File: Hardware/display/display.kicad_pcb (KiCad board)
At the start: 2 copper layers, 30.5 x 25.4 mm, 5 parts, among them J1 CONN_01X08, J2 CONN_01X08

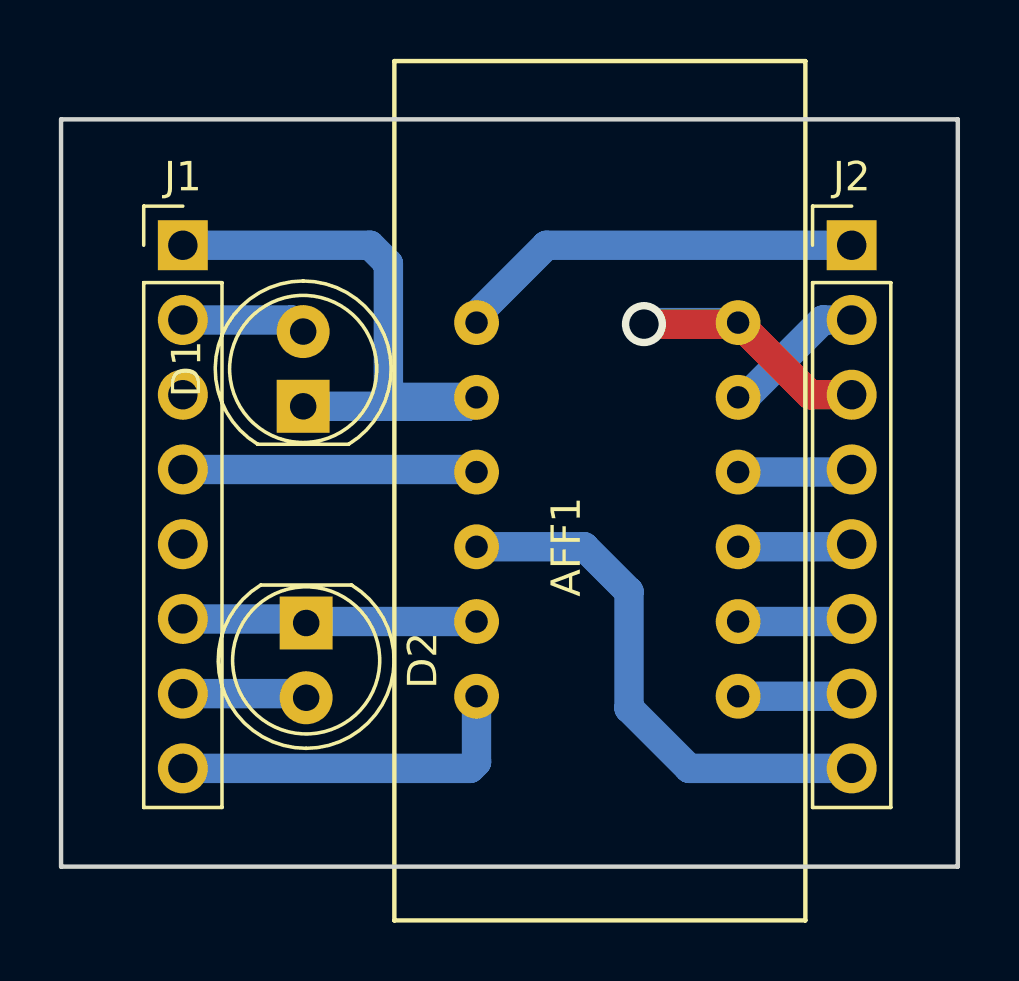
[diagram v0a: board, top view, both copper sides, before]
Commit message: Added 2 more LEDs
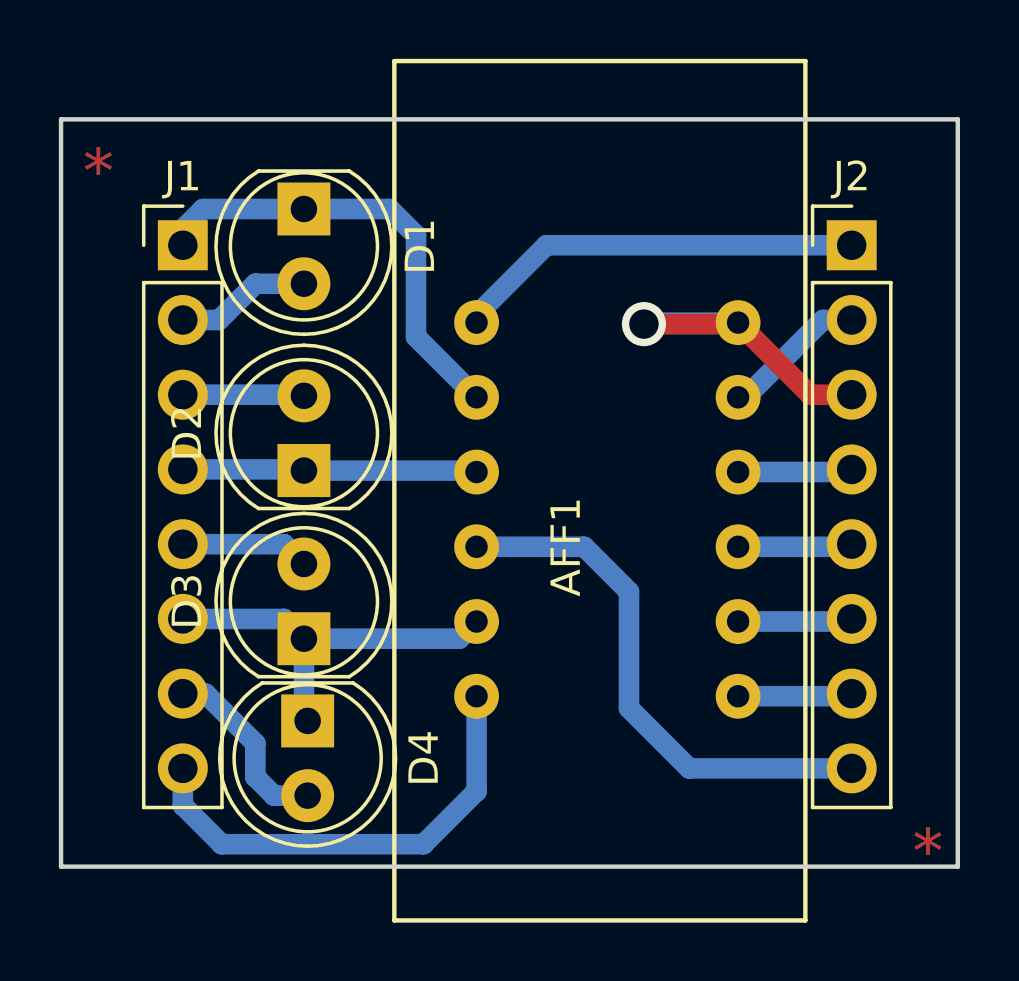
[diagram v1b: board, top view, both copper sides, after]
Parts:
- added D3: LED, LEDs:LED_D5.0mm, F.Cu at (31.1, 63.4)
- added D4: LED, LEDs:LED_D5.0mm, F.Cu at (31.2, 66.2)
- moved D1 6.71 mm to (31.1, 48.8), turned to 270 degrees
- moved D2 5.18 mm to (31.1, 57.7), turned to 90 degrees
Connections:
- D2 pad 1: /C2 -> /C4
- D2 pad 2: /A7 -> /A6
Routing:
- net /C1: track 20.8 -> 15.5 mm
- net /A1: track 0.00 -> 4.39 mm
- net /A6: track 0.00 -> 4.13 mm
- net /A8: track 12.3 -> 16.4 mm
- net /C2: track 10.0 -> 13.3 mm
- net /A7: track 4.25 -> 6.35 mm
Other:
- net class Default: trace_width 1 -> 0.7
- board text added: "*"
